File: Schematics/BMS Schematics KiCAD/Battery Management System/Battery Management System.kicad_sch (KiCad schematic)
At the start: 60 parts, among them J2 Boot, Q1 IRF9540NSTRLPBF, Q10 IRF9540NSTRLPBF, Q11 2N7002, Q12 IRF9540NSTRLPBF, Q13 2N7002, Q14 IRF9540NSTRLPBF, Q15 BSS84, Q16 2N7002, Q17 2N7002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

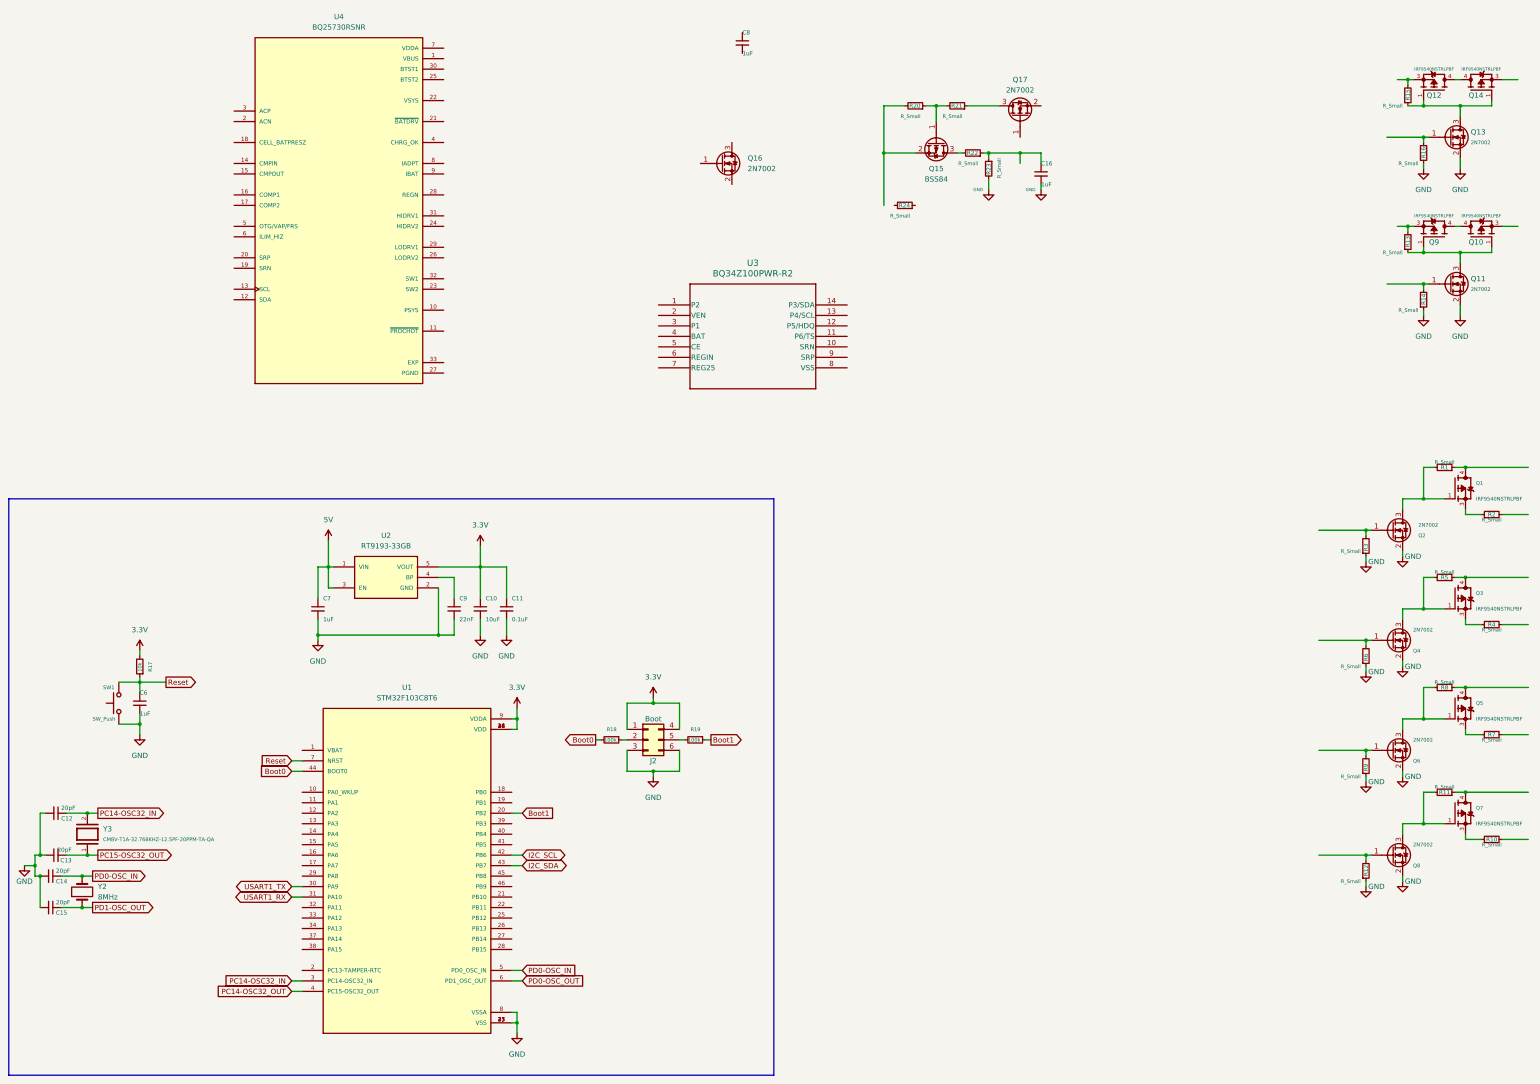
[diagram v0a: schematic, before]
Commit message: Add files via upload
This file contains the 2nd iteration of the Schematic of our Battery Management System.
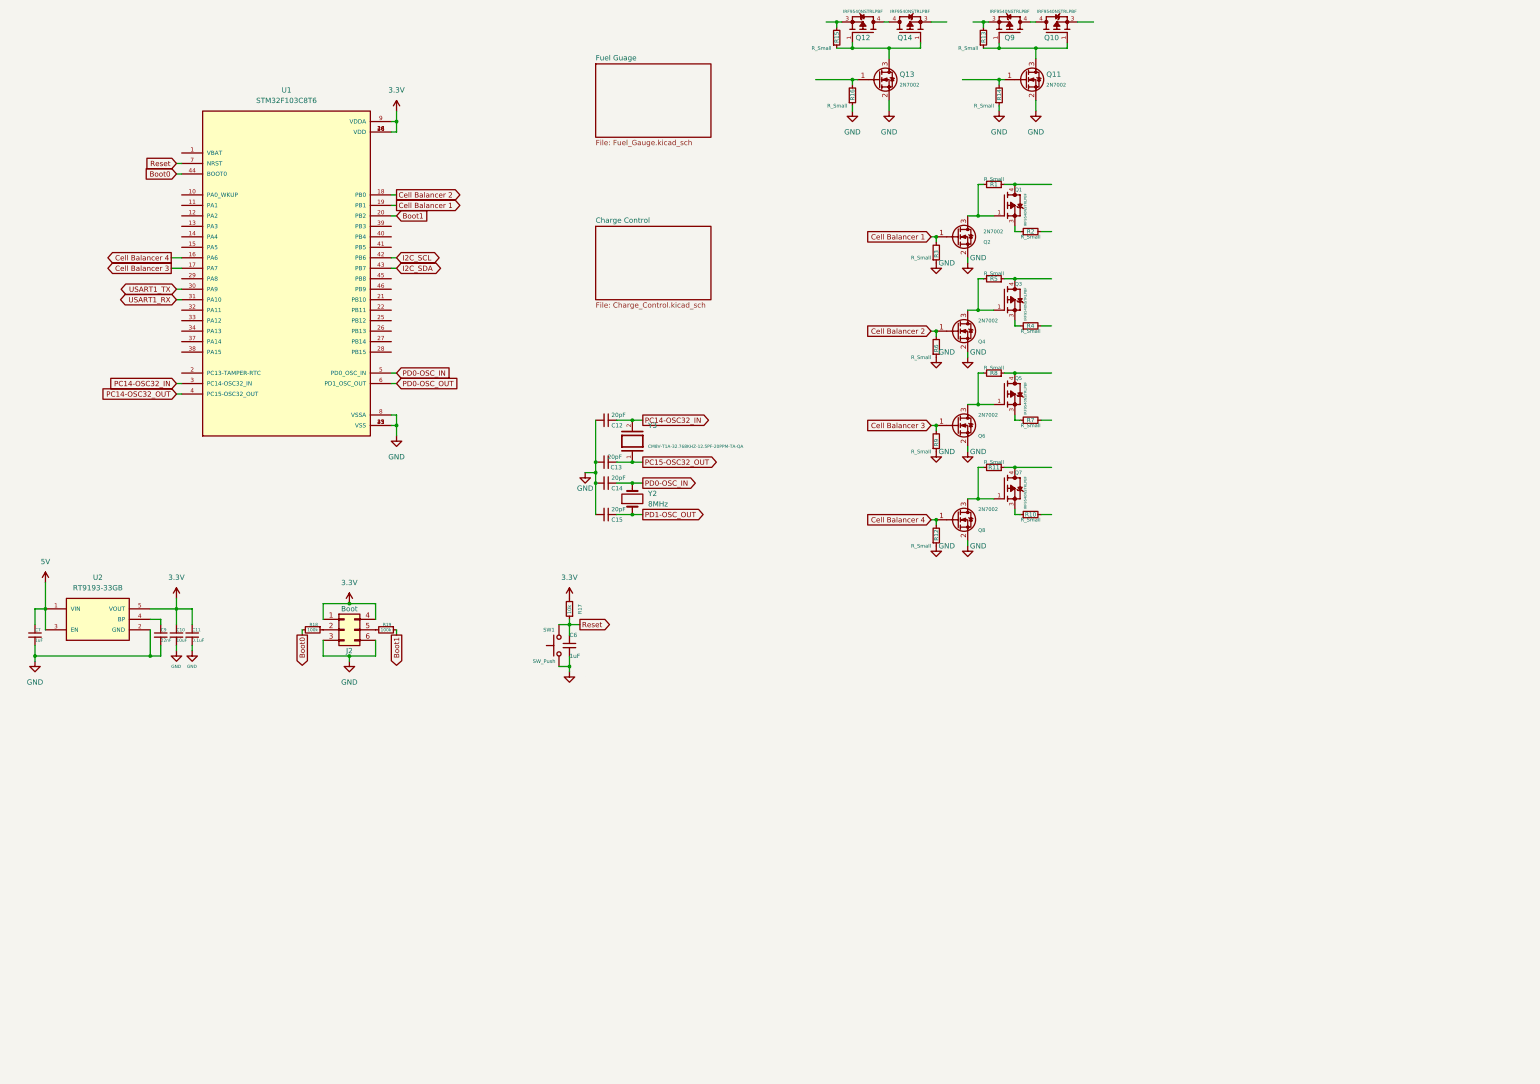
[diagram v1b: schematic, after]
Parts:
- removed C16, C8: 1uF, Capacitor_SMD:C_0201_0603Metric, symbol Device:C_Small
- removed Q15: BSS84, Package_TO_SOT_SMD:SOT-23, symbol Transistor_FET:BSS84
- removed Q16, Q17: 2N7002, Package_TO_SOT_SMD:SOT-23, symbol Transistor_FET:2N7002
- removed R20, R21, R22, R23, R24: R_Small, Resistor_SMD:R_0201_0603Metric, symbol Device:R_Small
- removed U3: BQ34Z100PWR-R2, BQ34Z100PWR-R2:PW14_TEX, symbol BQ34Z100PWR-R2:BQ34Z100PWR-R2
- removed U4: BQ25730RSNR, BQ25730RSNR:IC_BQ25730RSNR, symbol BQ25730RSNR:BQ25730RSNR
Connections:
- net Cell Balancer 2: now reaches Q4.1 (G), R6.2
- net Cell Balancer 2: now also U1.18 (PB0)
- net Cell Balancer 4: now reaches Q8.1 (G), R12.2
- net Cell Balancer 4: now also U1.16 (PA6)
- net Cell Balancer 1: now reaches Q2.1 (G), R3.2
- net Cell Balancer 1: now also U1.19 (PB1)
- net Cell Balancer 3: now reaches U1.17 (PA7)
- net Cell Balancer 3: now also Q6.1 (G), R9.2
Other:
- added sheet Charge Control (Charge_Control.kicad_sch)
- added sheet Fuel Guage (Fuel_Gauge.kicad_sch)
- moved on the sheet: C10, C11, C12, C13, C14, C15, C6, C7, C9, J2, Q1, Q10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

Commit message: Add files via upload
Latest iteration of KiCAD schematic for Battery Management System
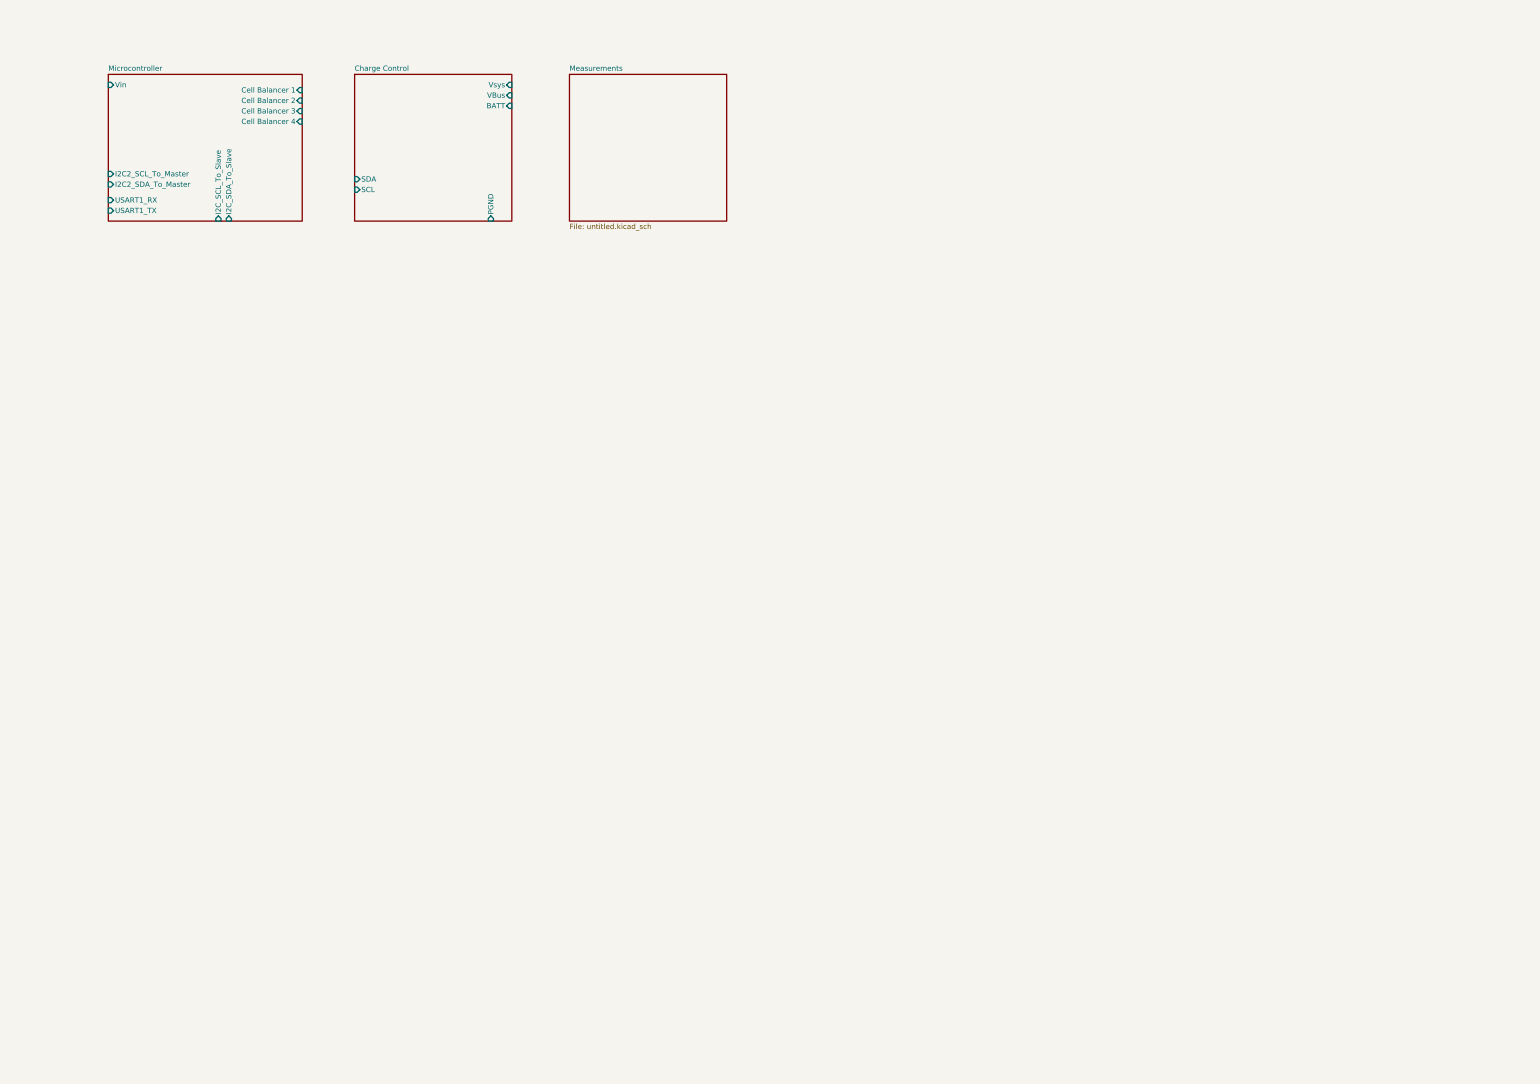
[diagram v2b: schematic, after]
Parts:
- removed C10: 10uF, Capacitor_SMD:C_0201_0603Metric, symbol Device:C_Small
- removed C11: 0.1uF, Capacitor_SMD:C_0201_0603Metric, symbol Device:C_Small
- removed C12, C13, C14, C15: 20pF, Capacitor_SMD:C_0201_0603Metric, symbol Device:C_Small
- removed C6, C7: 1uF, Capacitor_SMD:C_0201_0603Metric, symbol Device:C_Small
- removed C9: 22nF, Capacitor_SMD:C_0201_0603Metric, symbol Device:C_Small
- removed J2: Boot, symbol Connector_Generic:Conn_02x03_Top_Bottom
- removed Q1, Q10, Q12, Q14, Q3, Q5, Q7, Q9: IRF9540NSTRLPBF, IRF9540NSTRLPBF:DPAK254P1524X483-4_3N, symbol IRF9540NSTRLPBF:IRF9540NSTRLPBF
- removed Q11, Q13, Q2, Q4, Q6, Q8: 2N7002, Package_TO_SOT_SMD:SOT-23, symbol Transistor_FET:2N7002
- removed R1, R10, R11, R13, R15, R2, R4, R5, R7, R8: R_Small, symbol Device:R_Small
- removed R12, R14, R16, R3, R6, R9: R_Small, Resistor_SMD:R_0201_0603Metric, symbol Device:R_Small
- removed R17: 10k, Resistor_SMD:R_0201_0603Metric, symbol Device:R_Small
- removed R18, R19: 100k, Resistor_SMD:R_0201_0603Metric, symbol Device:R_Small
- removed SW1: SW_Push, symbol Switch:SW_Push
- removed U1: STM32F103C8T6, STM32F103C8T6:QFP50P900X900X160-48N, symbol STM32F103C8T6:STM32F103C8T6
- removed U2: RT9193-33GB, Package_TO_SOT_SMD:SOT-23-5, symbol RT9193-33GB:RT9193-33GB
- removed Y2: 8MHz, Crystal:Crystal_HC49-4H_Vertical, symbol Device:Crystal
- removed Y3: CM8V-T1A-32.768KHZ-12.5PF-20PPM-TA-QA, CM8V-T1A-32.768KHZ:XTAL_CM8V-T1A-32.768KHZ-12.5PF-20PPM-TA-QA, symbol CM8V-T1A-32.768KHZ-12.5PF-20PPM-TA-QA:CM8V-T1A-32.768KHZ-12.5PF-20PPM-TA-QA
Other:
- removed sheet Fuel Guage
- added sheet Measurements (untitled.kicad_sch)
- added sheet Microcontroller (Microcontroller.kicad_sch)
- sheet Charge Control ports: added BATT, PGND, SCL, SDA, VBus, Vsys; removed none

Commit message: Pulled together root sheet so that it's obvious how the power flows and how the blocks are connected. Finally, a decent block diagram :)
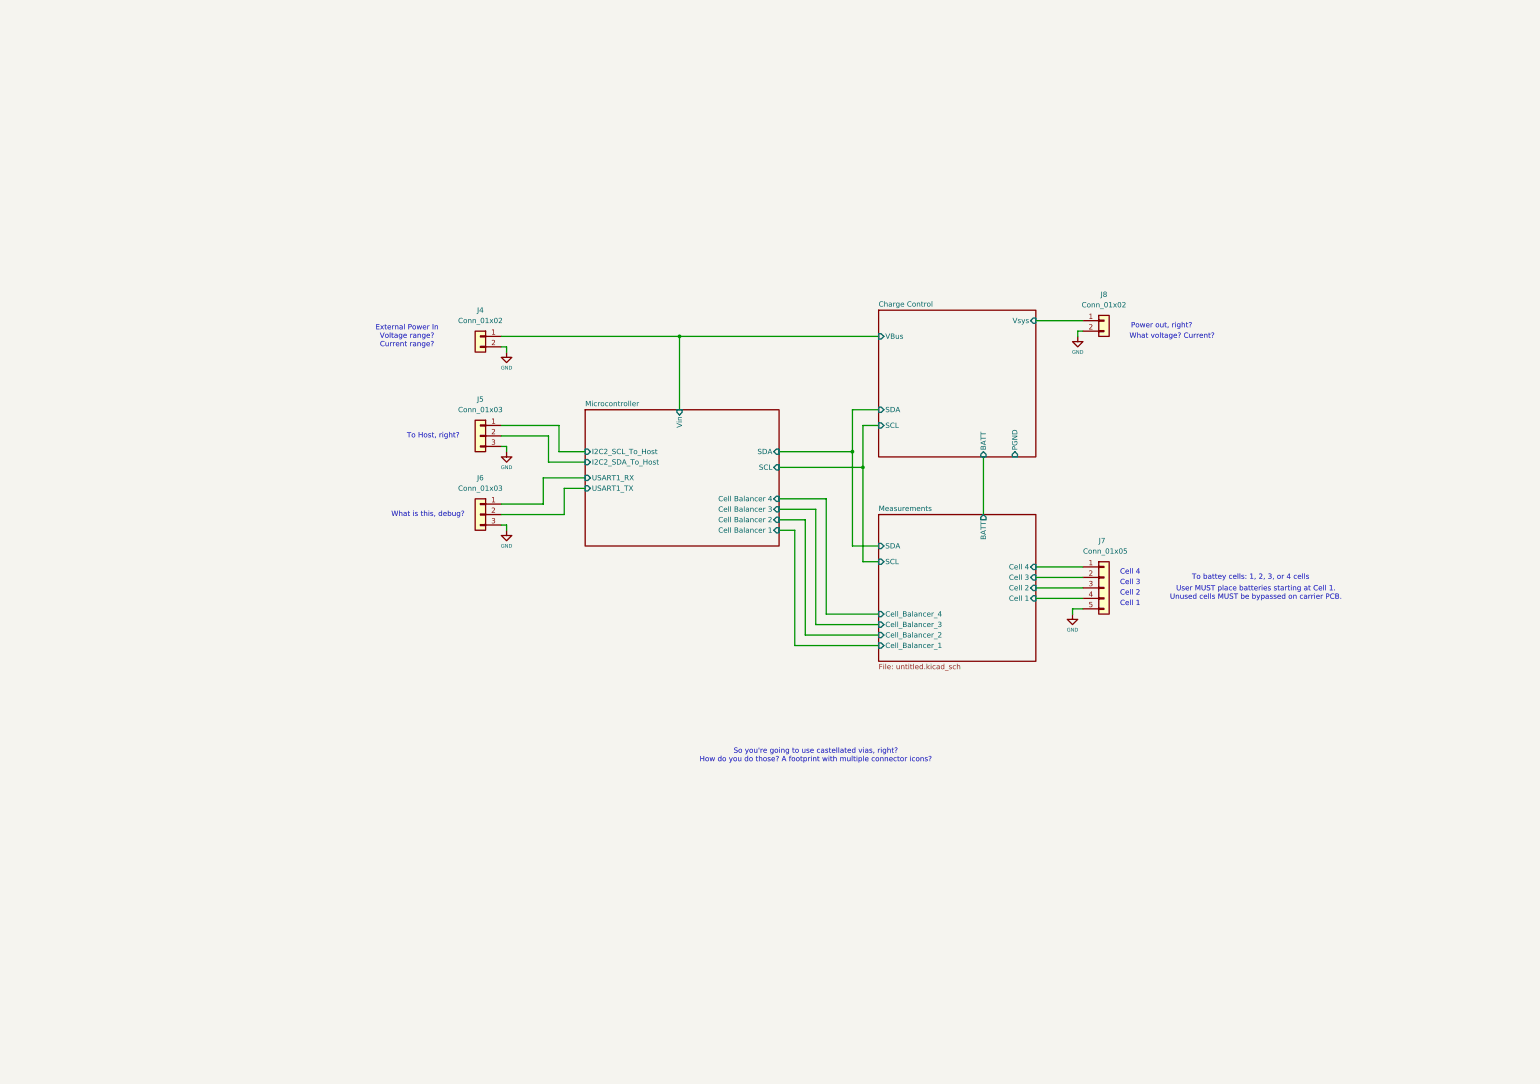
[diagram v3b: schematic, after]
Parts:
- added J4, J8: Conn_01x02, symbol Connector_Generic:Conn_01x02
- added J5, J6: Conn_01x03, symbol Connector_Generic:Conn_01x03
- added J7: Conn_01x05, symbol Connector_Generic:Conn_01x05
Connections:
- net Charge Control/VBus: now also J4.1 (Pin_1)
- net Charge Control/Vsys: now also J8.1 (Pin_1)
- net Microcontroller/USART1_RX: now also J6.1 (Pin_1)
- net Microcontroller/USART1_TX: now also J6.2 (Pin_2)
- new net GND: J4.2 (Pin_2), J5.3 (Pin_3), J6.3 (Pin_3), J7.5 (Pin_5), J8.2 (Pin_2)
- new net Measurements/Cell 1: J7.4 (Pin_4)
- new net Measurements/Cell 2: J7.3 (Pin_3)
- new net Measurements/Cell 3: J7.2 (Pin_2)
- new net Measurements/Cell 4: J7.1 (Pin_1)
- new net Microcontroller/I2C2_SCL_To_Host: J5.1 (Pin_1)
- new net Microcontroller/I2C2_SDA_To_Host: J5.2 (Pin_2)
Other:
- sheet Measurements ports: added BATT, Cell 1, Cell 2, Cell 3, Cell 4, Cell_Balancer_1, Cell_Balancer_2, Cell_Balancer_3, Cell_Balancer_4, SCL, SDA; removed none
- sheet Microcontroller ports: added I2C2_SCL_To_Host, I2C2_SDA_To_Host, SCL, SDA; removed I2C2_SCL_To_Master, I2C2_SDA_To_Master, I2C_SCL_To_Slave , I2C_SDA_To_Slave
- note added: "Cell 1"
- note added: "Cell 2"
- note added: "Cell 3"
- note added: "Cell 4"
- note added: "External Power In Voltage range? Current range?"
- note added: "Power out, right?"
- note added: "So you're going to use castellated vias, right? How do you do those? A footprint with multiple connector icons?"
- note added: "To Host, right?"
- note added: "To battey cells: 1, 2, 3, or 4 cells"
- note added: "User MUST place batteries starting at Cell 1. Unused cells MUST be bypassed on carrier PCB."
- note added: "What is this, debug?"
- note added: "What voltage? Current?"

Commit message: Renamed untitled to Cell Interface
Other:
- sheet Measurements renamed Cell Interface
- sheet Cell Interface: file untitled.kicad_sch -> Cell_Interface.kicad_sch
- note added: "SYSTEM OVERVIEW HERE PLZ"
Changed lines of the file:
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@@
+		)
+	)
+	(text "SYSTEM OVERVIEW HERE PLZ"
+		(exclude_from_sim no)
+		(at 176.53 67.31 0)
+		(effects
+			(font
+				(size 1.27 1.27)
+			)
 		)
 	)
@@
 			(color 255 232 188 1.0000)
 		)
-		(property "Sheetname" "Measurements"
+		(property "Sheetname" "Cell Interface"
 			(at 224.79 146.6084 0)
 			(effects
@@
 			)
 		)
-		(property "Sheetfile" "untitled.kicad_sch"
+		(property "Sheetfile" "Cell_Interface.kicad_sch"
 			(at 224.79 183.4646 0)
 			(effects
